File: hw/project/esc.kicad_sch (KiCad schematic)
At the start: 0 parts

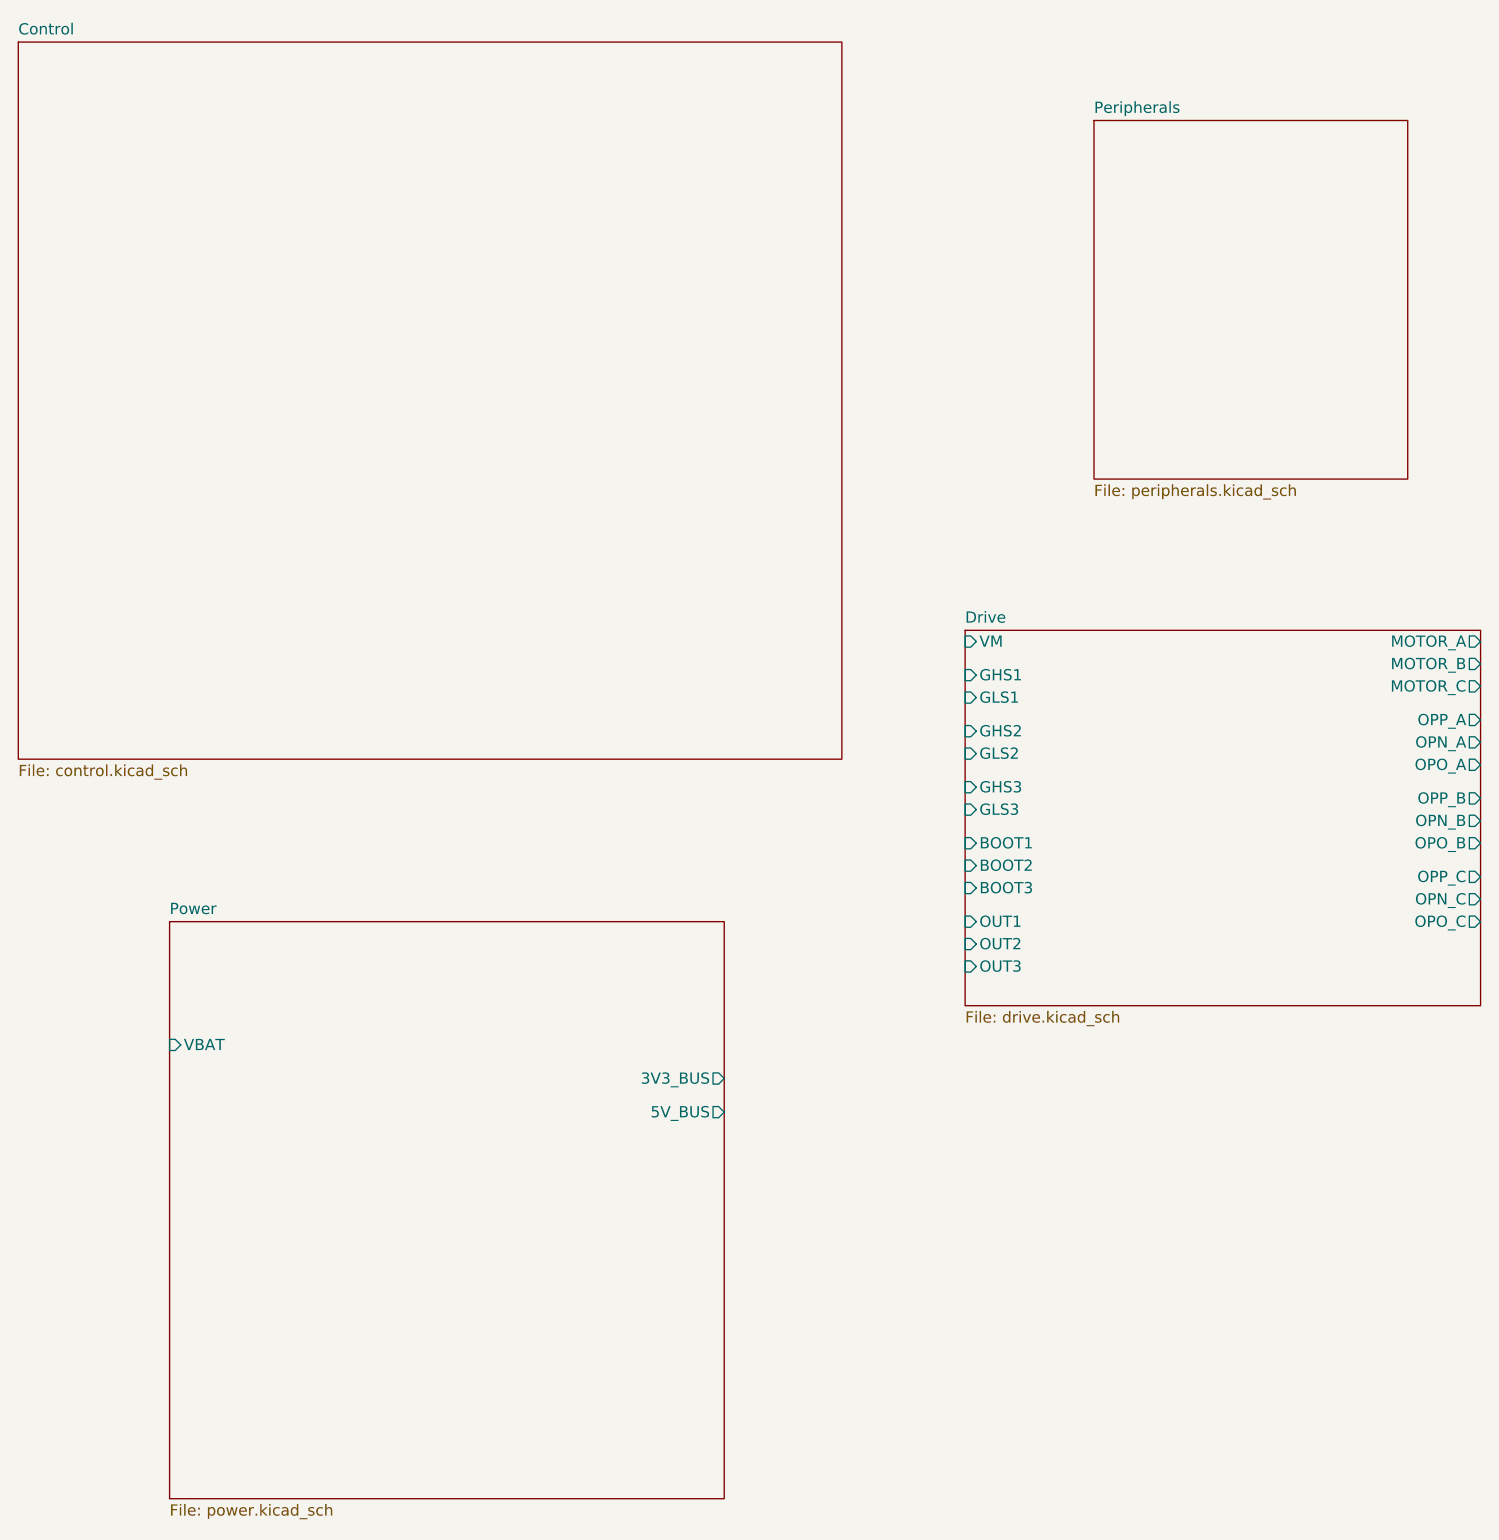
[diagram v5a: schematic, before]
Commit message: Updated local/hierarchical labels, renamed signals, and added alternate pin functions. Still need to review application circuit values fr.
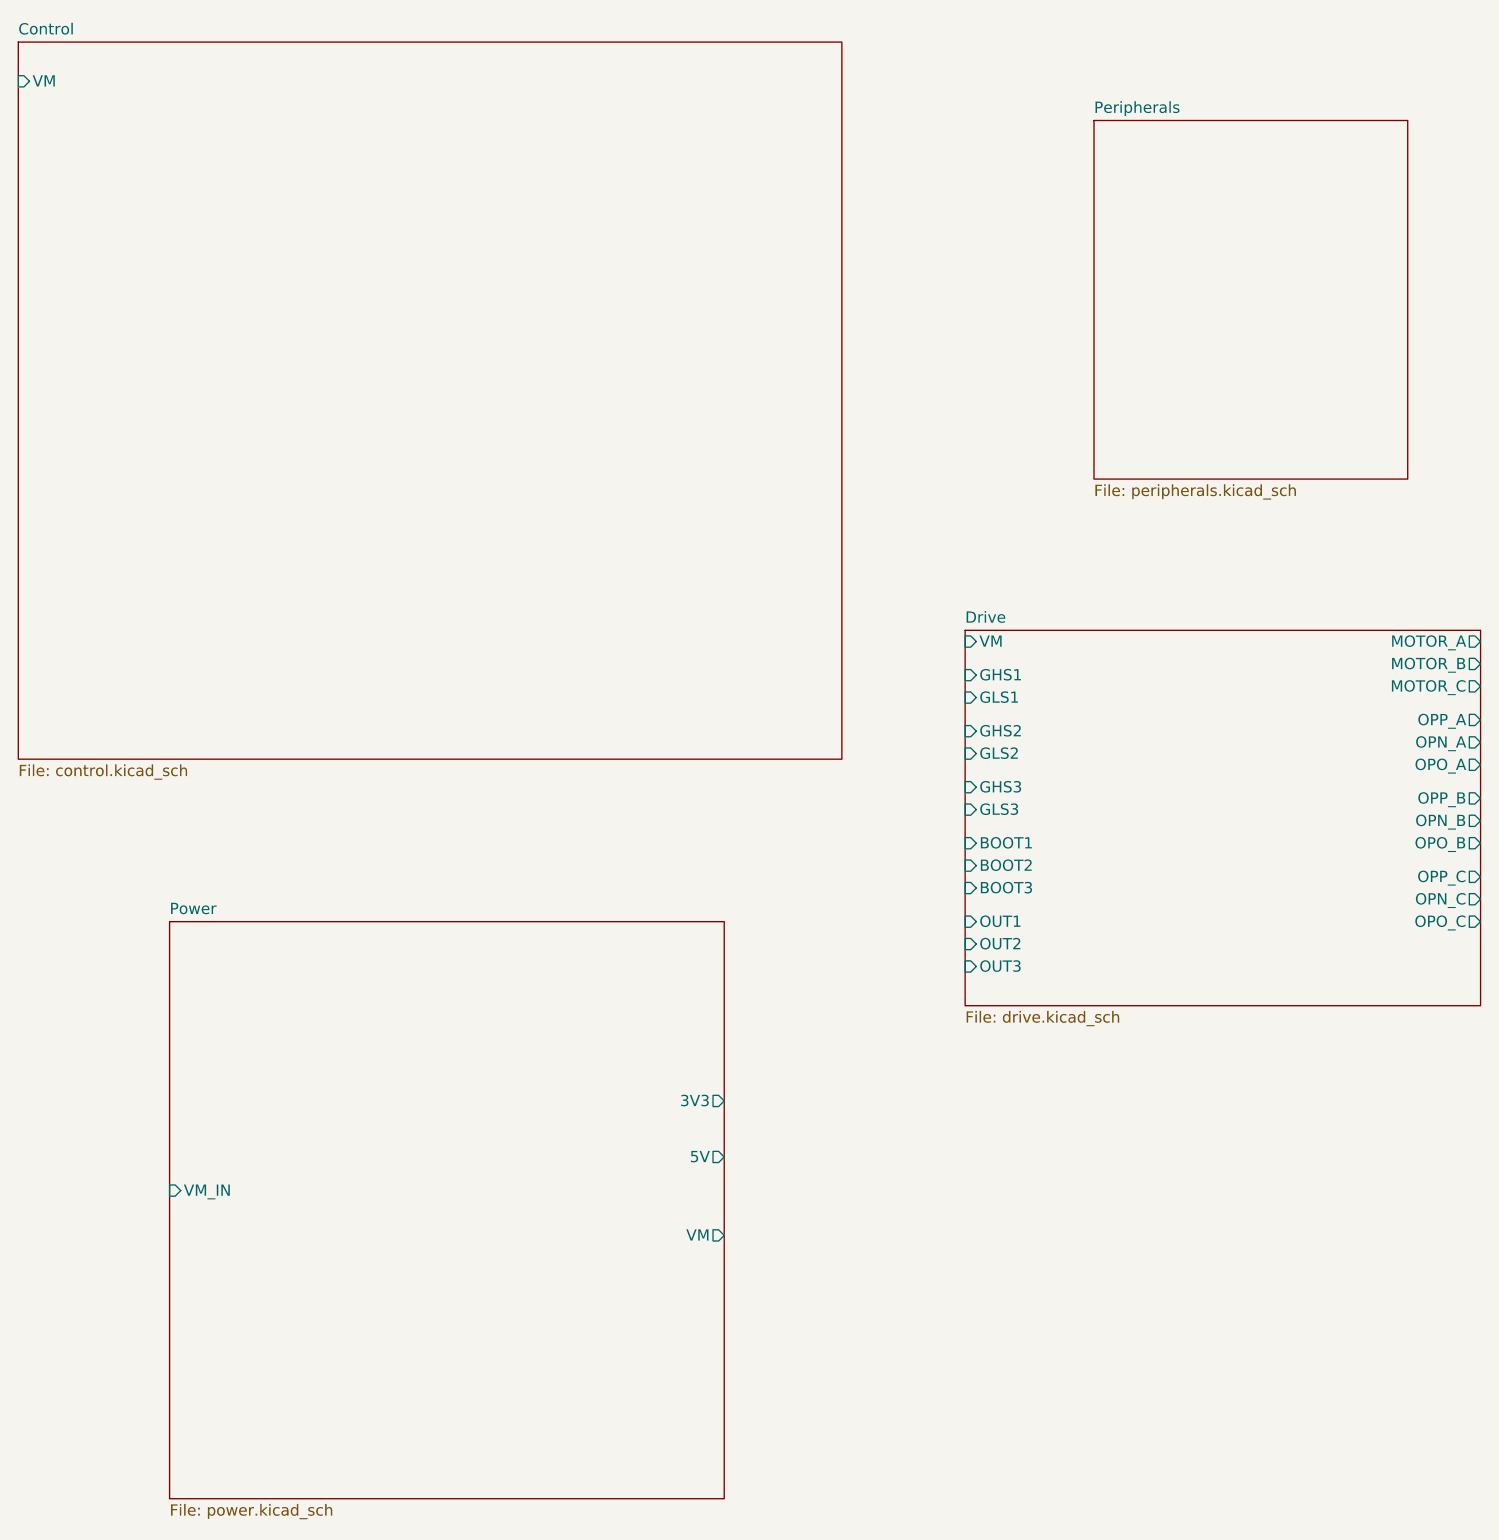
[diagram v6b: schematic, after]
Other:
- sheet Control ports: added VM; removed none
- sheet Power ports: added 3V3, 5V, VM, VM_IN; removed 3V3_BUS, 5V_BUS, VBAT
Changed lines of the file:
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@@
+			)
+		)
+		(pin "VM" input
+			(at 13.335 20.32 180)
+			(effects
+				(font
+					(size 1.27 1.27)
+				)
+				(justify left)
 			)
 		)
@@
 			)
 		)
-		(pin "VBAT" input
-			(at 30.48 129.54 180)
+		(pin "3V3" output
+			(at 93.345 135.89 0)
+			(effects
+				(font
+					(size 1.27 1.27)
+				)
+				(justify right)
+			)
+		)
+		(pin "5V" output
+			(at 93.345 142.24 0)
+			(effects
+				(font
+					(size 1.27 1.27)
+				)
+				(justify right)
+			)
+		)
+		(pin "VM" output
+			(at 93.345 151.13 0)
+			(effects
+				(font
+					(size 1.27 1.27)
+				)
+				(justify right)
+			)
+		)
+		(pin "VM_IN" input
+			(at 30.48 146.05 180)
 			(effects
 				(font
@@
 			)
 		)
-		(pin "3V3_BUS" output
-			(at 93.345 133.35 0)
-			(effects
-				(font
-					(size 1.27 1.27)
-				)
-				(justify right)
-			)
-		)
-		(pin "5V_BUS" output
-			(at 93.345 137.16 0)
-			(effects
-				(font
-					(size 1.27 1.27)
-				)
-				(justify right)
-			)
-		)

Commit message: Clean up control sheet (no boxes yet)
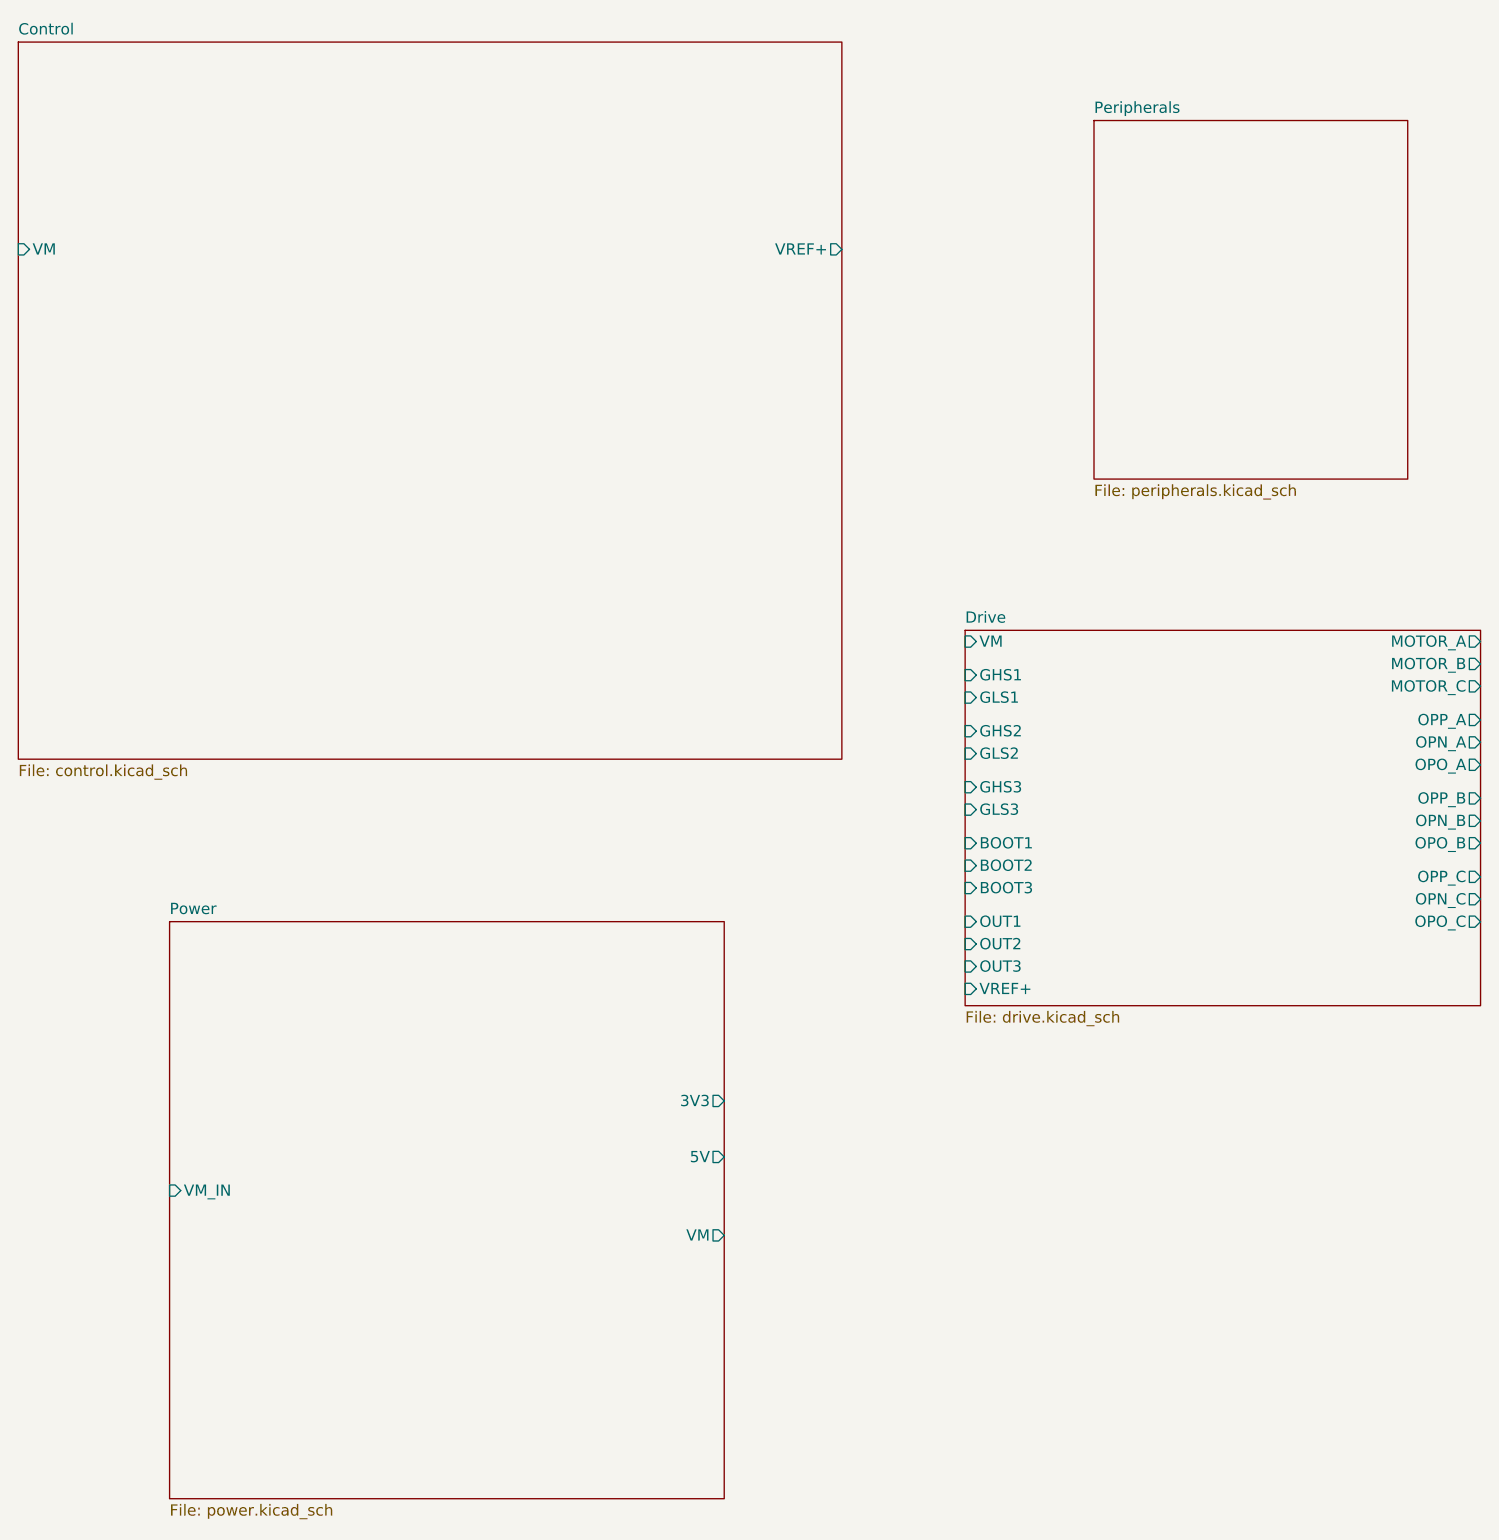
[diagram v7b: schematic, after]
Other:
- sheet Control ports: added VREF+; removed none
- sheet Drive ports: added VREF+; removed none
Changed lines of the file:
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@@
 		)
 		(pin "VM" input
-			(at 13.335 20.32 180)
-			(effects
-				(font
-					(size 1.27 1.27)
-				)
-				(justify left)
+			(at 13.335 39.37 180)
+			(effects
+				(font
+					(size 1.27 1.27)
+				)
+				(justify left)
+			)
+		)
+		(pin "VREF+" output
+			(at 106.68 39.37 0)
+			(effects
+				(font
+					(size 1.27 1.27)
+				)
+				(justify right)
 			)
 		)
@@
 			)
 		)
+		(pin "VREF+" input
+			(at 120.65 123.19 180)
+			(effects
+				(font
+					(size 1.27 1.27)
+				)
+				(justify left)
+			)
+		)

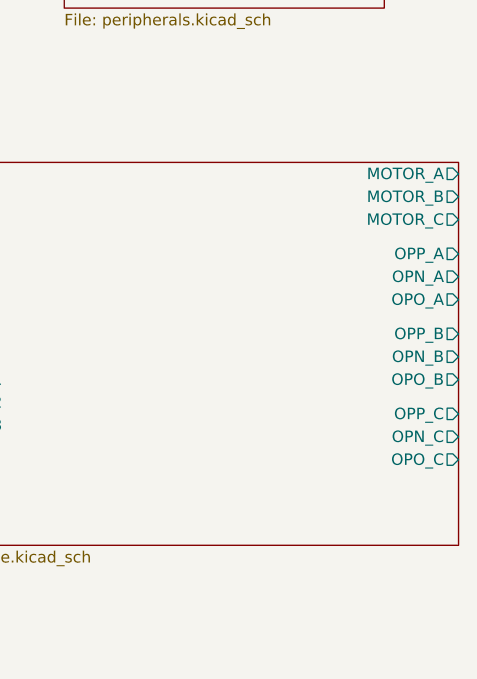
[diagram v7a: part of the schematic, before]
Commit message: Update phase labels and organize half bridges
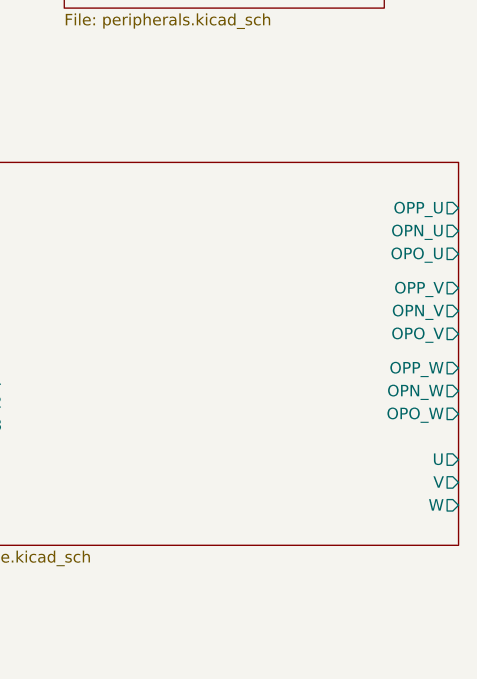
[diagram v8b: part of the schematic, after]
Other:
- sheet Drive ports: added OPN_U, OPN_V, OPN_W, OPO_U, OPO_V, OPO_W, OPP_U, OPP_V, OPP_W, U, V, W; removed MOTOR_A, MOTOR_B, MOTOR_C, OPN_A, OPN_B, OPN_C, OPO_A, OPO_B, OPO_C, OPP_A, OPP_B, OPP_C
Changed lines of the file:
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@@
-			)
-		)
-		(pin "MOTOR_C" output
-			(at 179.07 88.9 0)
-			(effects
-				(font
-					(size 1.27 1.27)
-				)
-				(justify right)
 			)
 		)
@@
 			)
 		)
-		(pin "MOTOR_A" output
-			(at 179.07 83.82 0)
-			(effects
-				(font
-					(size 1.27 1.27)
-				)
-				(justify right)
-			)
-		)
 		(pin "GLS2" input
 			(at 120.65 96.52 180)
@@
 			)
 		)
-		(pin "MOTOR_B" output
-			(at 179.07 86.36 0)
-			(effects
-				(font
-					(size 1.27 1.27)
-				)
-				(justify right)
-			)
-		)
 		(pin "OUT2" input
 			(at 120.65 118.11 180)
@@
 			)
 		)
-		(pin "OPN_A" output
-			(at 179.07 95.25 0)
-			(effects
-				(font
-					(size 1.27 1.27)
-				)
-				(justify right)
-			)
-		)
-		(pin "OPO_A" output
-			(at 179.07 97.79 0)
-			(effects
-				(font
-					(size 1.27 1.27)
-				)
-				(justify right)
-			)
-		)
-		(pin "OPO_B" output
-			(at 179.07 106.68 0)
-			(effects
-				(font
-					(size 1.27 1.27)
-				)
-				(justify right)
-			)
-		)
-		(pin "OPP_A" output
-			(at 179.07 92.71 0)
-			(effects
-				(font
-					(size 1.27 1.27)
-				)
-				(justify right)
-			)
-		)
-		(pin "OPO_C" output
-			(at 179.07 115.57 0)
-			(effects
-				(font
-					(size 1.27 1.27)
-				)
-				(justify right)
-			)
-		)
-		(pin "OPN_B" output
-			(at 179.07 104.14 0)
-			(effects
-				(font
-					(size 1.27 1.27)
-				)
-				(justify right)
-			)
-		)
-		(pin "OPP_B" output
-			(at 179.07 101.6 0)
-			(effects
-				(font
-					(size 1.27 1.27)
-				)
-				(justify right)
-			)
-		)
-		(pin "OPN_C" output
-			(at 179.07 113.03 0)
-			(effects
-				(font
-					(size 1.27 1.27)
-				)
-				(justify right)
-			)
-		)
-		(pin "OPP_C" output
-			(at 179.07 110.49 0)
-			(effects
-				(font
-					(size 1.27 1.27)
-				)
-				(justify right)
-			)
-		)
 		(pin "VREF+" input
 			(at 120.65 123.19 180)
@@
 			)
 		)
+		(pin "OPP_V" output
+			(at 179.07 96.52 0)
+			(effects
+				(font
+					(size 1.27 1.27)
+				)
+				(justify right)
+			)
+		)
+		(pin "OPO_W" output
+			(at 179.07 110.49 0)
+			(effects
+				(font
+					(size 1.27 1.27)
+				)
+				(justify right)
+			)
+		)
+		(pin "OPP_U" output
+			(at 179.07 87.63 0)
+			(effects
+				(font
+					(size 1.27 1.27)
+				)
+				(justify right)
+			)
+		)
+		(pin "OPN_U" output
+			(at 179.07 90.17 0)
+			(effects
+				(font
+					(size 1.27 1.27)
+				)
+				(justify right)
+			)
+		)
+		(pin "U" output
+			(at 179.07 115.57 0)
+			(effects
+				(font
+					(size 1.27 1.27)
+				)
+				(justify right)
+			)
+		)
+		(pin "OPP_W" output
+			(at 179.07 105.41 0)
+			(effects
+				(font
+					(size 1.27 1.27)
+				)
+				(justify right)
+			)
+		)
+		(pin "OPN_W" output
+			(at 179.07 107.95 0)
+			(effects
+				(font
+					(size 1.27 1.27)
+				)
+				(justify right)
+			)
+		)
+		(pin "V" output
+			(at 179.07 118.11 0)
+			(effects
+				(font
+					(size 1.27 1.27)
+				)
+				(justify right)
+			)
+		)
+		(pin "OPO_V" output
+			(at 179.07 101.6 0)
+			(effects
+				(font
+					(size 1.27 1.27)
+				)
+				(justify right)
+			)
+		)
+		(pin "OPN_V" output
+			(at 179.07 99.06 0)
+			(effects
+				(font
+					(size 1.27 1.27)
+				)
+				(justify right)
+			)
+		)
+		(pin "OPO_U" output
+			(at 179.07 92.71 0)
+			(effects
+				(font
+					(size 1.27 1.27)
+				)
+				(justify right)
+			)
+		)
+		(pin "W" output
+			(at 179.07 120.65 0)
+			(effects
+				(font
+					(size 1.27 1.27)
+				)
+				(justify right)
+			)
+		)
